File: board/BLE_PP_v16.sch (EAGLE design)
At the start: 18 parts, among them SW4 SW_SLIDECUS12B, U1 MOD_CYBLE014008-00, U2 REG_TPS61221

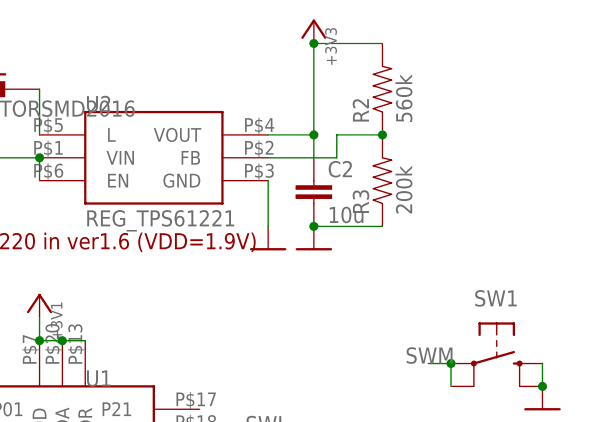
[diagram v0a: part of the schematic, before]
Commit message: スリープに入るアルゴリズム＆L2CAP paramUpdateRequestを送るアルゴリズムを変更。SleepからIDボタンで復帰。マニュアルの修正。
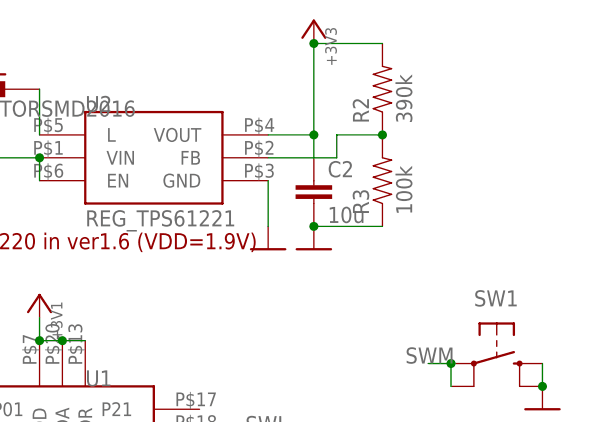
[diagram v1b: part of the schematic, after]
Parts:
- R2: value 560k -> 390k
- R3: value 200k -> 100k
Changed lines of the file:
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@@
 <?xml version="1.0" encoding="utf-8"?>
 <!DOCTYPE eagle SYSTEM "eagle.dtd">
-<eagle version="8.1.0">
+<eagle version="7.7.0">
 <drawing>
 <settings>
@@
 <part name="L1" library="akita" deviceset="INDUCTOR" device="SMD2016" value="INDUCTORSMD2016"/>
 <part name="SW6" library="akita" deviceset="SW_TACT" device="EVQP7"/>
-<part name="R2" library="akita" deviceset="RES" device="0603" value="560k"/>
-<part name="R3" library="akita" deviceset="RES" device="0603" value="200k"/>
+<part name="R2" library="akita" deviceset="RES" device="0603" value="390k"/>
+<part name="R3" library="akita" deviceset="RES" device="0603" value="100k"/>
 </parts>
 <sheets>
